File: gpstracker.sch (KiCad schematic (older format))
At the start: 16 parts, among them U1 ATMEGA328P-AU

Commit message: Major building blocks are there
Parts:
- added C?: 0.1uF, symbol C
- added ICSP: CONN_02X03, symbol CONN_02X03
- added J?: Micro_SD_Card, symbol Micro_SD_Card
- added J?: CONN_01X06, symbol CONN_01X06
- added R? (x2): 50k, symbol R
- C?: value 4.7uF -> 0.1uF
- R?: value 470R -> 10k
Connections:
- net labels added: ARD_HRX, ARD_HTX, ARD_IO10, ARD_IO7, ARD_IO8, ARD_IO9, ARD_MISO, ARD_MOSI, ARD_RST, ARD_RX, ARD_SCK, ARD_TX
- net labels removed: ARD_RXD, ARD_TXD
- wire segments 54 -> 116
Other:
- note added: "=> FTDI_VCC NOT VCC"
- note added: "SD card"

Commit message: Power supplies
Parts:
- added C? (x2): 1uF, symbol C
- added SW? (x2): SW_DPDT_x2, symbol SW_DPDT_x2
- added U?: MCP1700T-3302E/TT, symbol MCP1700T-3002E/TT
- D?: value LED -> CHRG
- D?: value LED -> DONE
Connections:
- net labels added: +3.3V, +3.3V_FDTI, +3.3V_REGUL
- net labels removed: VCC, VIN
- wire segments 116 -> 134
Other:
- note added: "GPS & GSM"
- note added: "Needs modifications for load sharing, as a starting point see :\nhttp://blog.zakkemble.co.uk/a-lithium-battery-charger-with-load-sharing/"
- note removed: "=> FTDI_VCC NOT VCC"
- note removed: "Needs modifications for load sharing, as a starting point see :\nsee http://blog.zakkemble.co.uk/a-lithium-battery-charger-with-load-sharing/"
- moved on the sheet: C?, D?, IC?, ICSP, J?, R?, SW?A, TV?, U1

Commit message: Circuitry is mostly done
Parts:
- removed J?: CONN_01X02, symbol CONN_01X02
- removed R?: 2k, symbol R
- removed R?: 470R, symbol R
- removed R?: 1k, symbol R
- removed R?: 10k, symbol R
- removed SW? (x2): SW_DPDT_x2, symbol SW_DPDT_x2
- added BT? (x2): Battery_Cell, symbol Battery_Cell
- added C? (x2): C, symbol C
- added C?: 10uF, symbol C
- added D?: D_Schottky, symbol D_Schottky
- added J? (x2): CONN_COAXIAL, symbol CONN_COAXIAL
- added J?: GS2, Connectors:GS2, symbol GS2
- added LED? (x3): LED, symbol LED
- added Q?: MOSFET_P, symbol MOSFET_P
- added R? (x2): 10k, symbol R
- added R? (x6): 1k, symbol R
- added R?: 20k, symbol R
- added R?: 160R, symbol R
- added R?: 2k, symbol R
- added R? (x2): 470R, symbol R
- added U?: 24LC512, SOIC-8_3.9x4.9mm_Pitch1.27mm, symbol 24LC512
- added U?: DS3231SN, Housings_SOIC:SOIC-16_7.5x10.3mm_Pitch1.27mm, symbol DS3231
- D? (x2): symbol LED -> LED-RESCUE-gpstracker
- R? (x2): symbol R -> R-RESCUE-gpstracker
- U?: symbol MCP73832-5-OT -> MCP73832-5-OT-RESCUE-gpstracker
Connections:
- net labels added: +2V8, +5V_FTDI, LED_NETWORK, LED_PWR, LED_SIM808_PWR, RTC_PWR, SCL, SDA, SIM808_P, SIM808_RI, SIM808_S, WAKE_UP
- net labels removed: +3.3V_FDTI, +3.3V_REGUL, ARD_IO7, ARD_IO8, ARD_IO9
- wire segments 134 -> 203
- no-connect marks 5 -> 48
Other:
- note added: "LEDs"
- note added: "Programming"
- note added: "RTC"
- note added: "Storage"
- note removed: "Needs modifications for load sharing, as a starting point see :\nhttp://blog.zakkemble.co.uk/a-lithium-battery-charger-with-load-sharing/"
- moved on the sheet: C?, D?, IC?, ICSP, J?, R?, SW?A, U1, U?

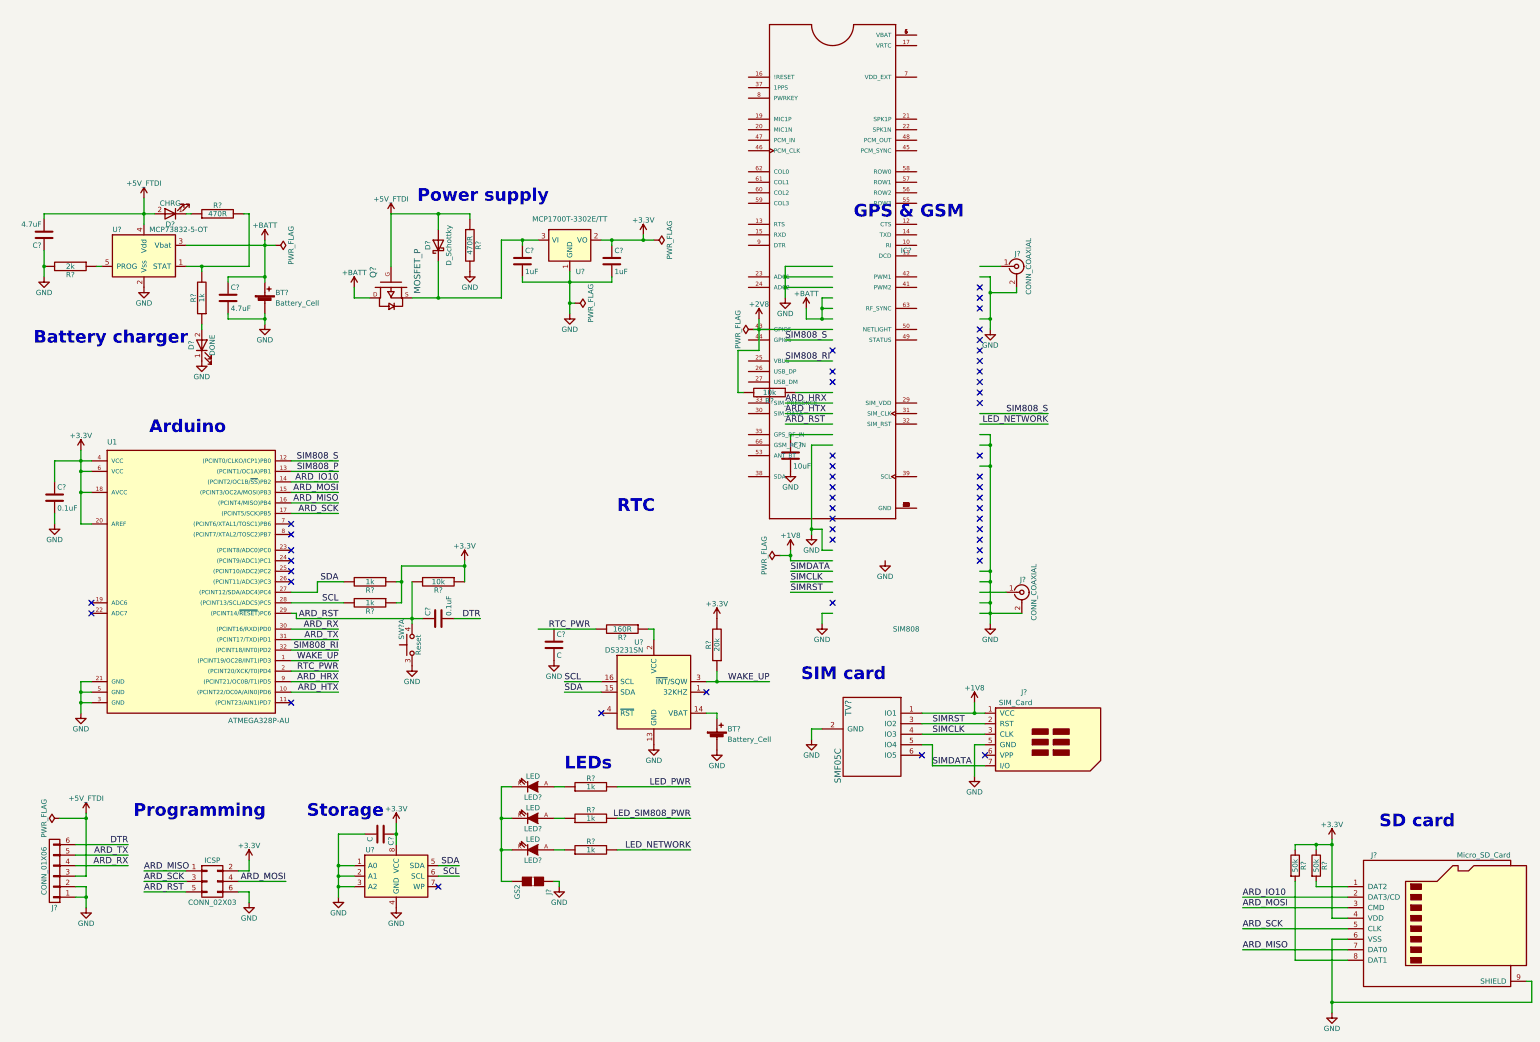
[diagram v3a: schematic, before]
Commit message: Replaced SIM808 lib with a better one
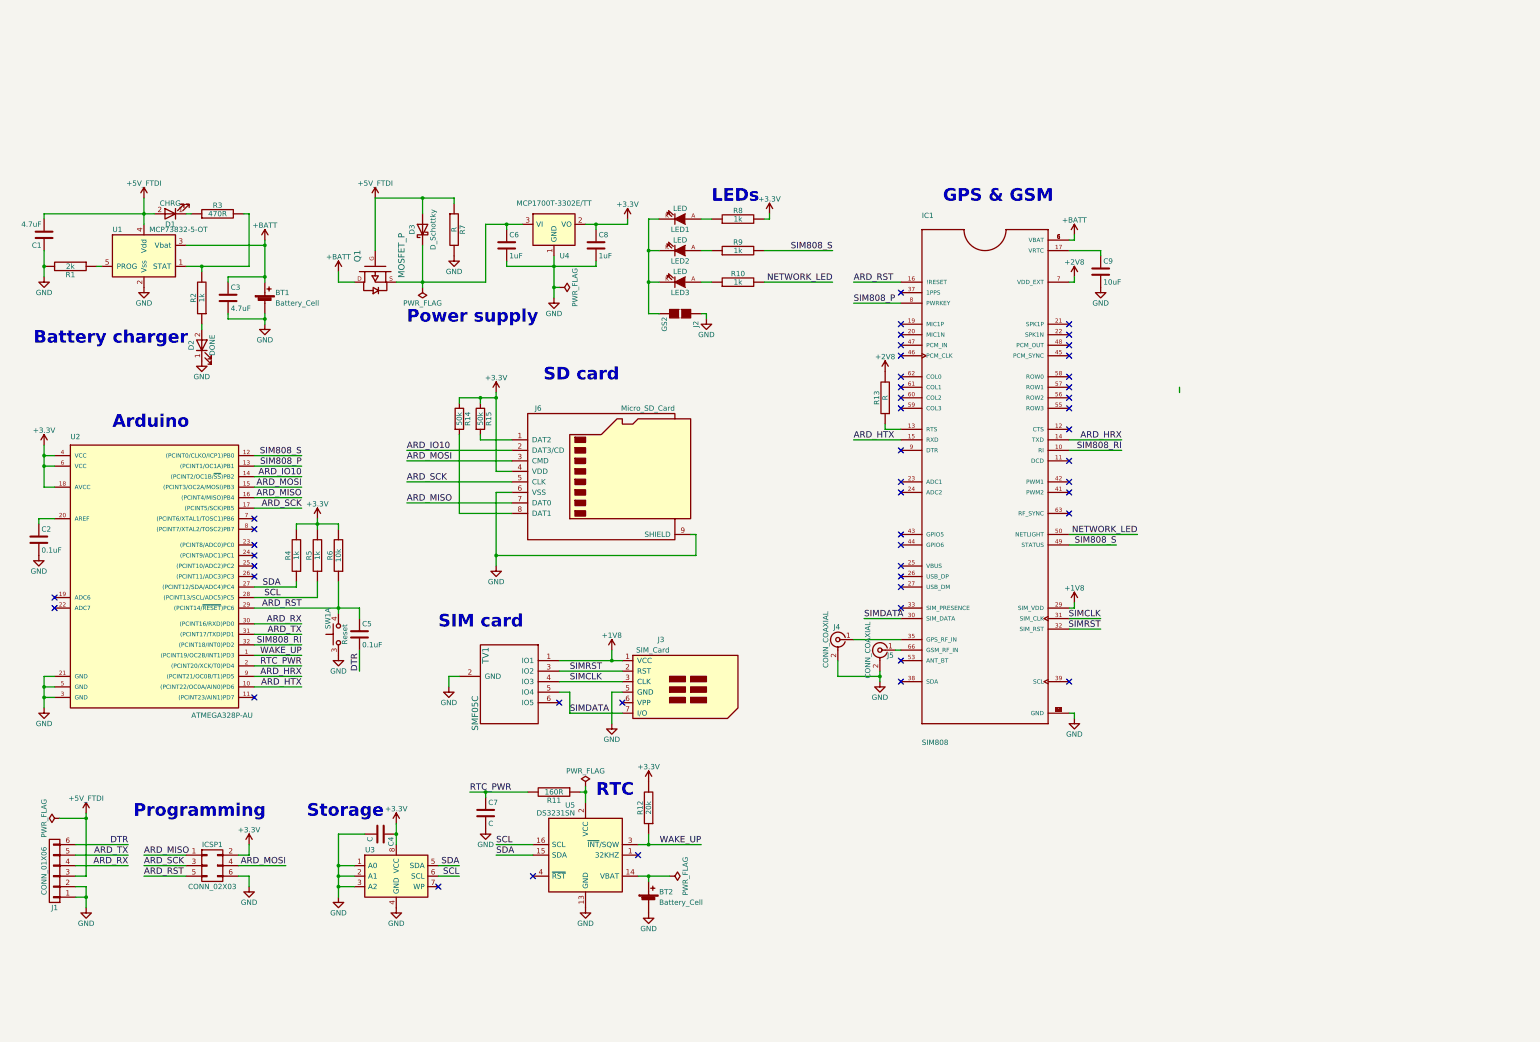
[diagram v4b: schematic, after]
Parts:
- removed C?: 10uF, symbol C
- removed IC?: SIM808, SIM808, symbol SIM808
- removed J? (x2): CONN_COAXIAL, symbol CONN_COAXIAL
- removed R?: 10k, symbol R
- added C9: 10uF, symbol C
- added IC1: SIM808, QFN100P2400X2400X260-68N, symbol SIM808
- added J4, J5: CONN_COAXIAL, symbol CONN_COAXIAL
- added R13: R, symbol R
- R7: renamed from R?; value 470R -> R
- gave numbers to parts that had none: 40
- renumbered ICSP to ICSP1, U1 to U2
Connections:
- net labels added: NETWORK_LED
- net labels removed: LED_NETWORK, LED_PWR, LED_SIM808_PWR
- wire segments 203 -> 178
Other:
- moved on the sheet: BT2, C2, C5, C6, C7, C8, D3, ICSP1, J2, J3, J6, LED1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

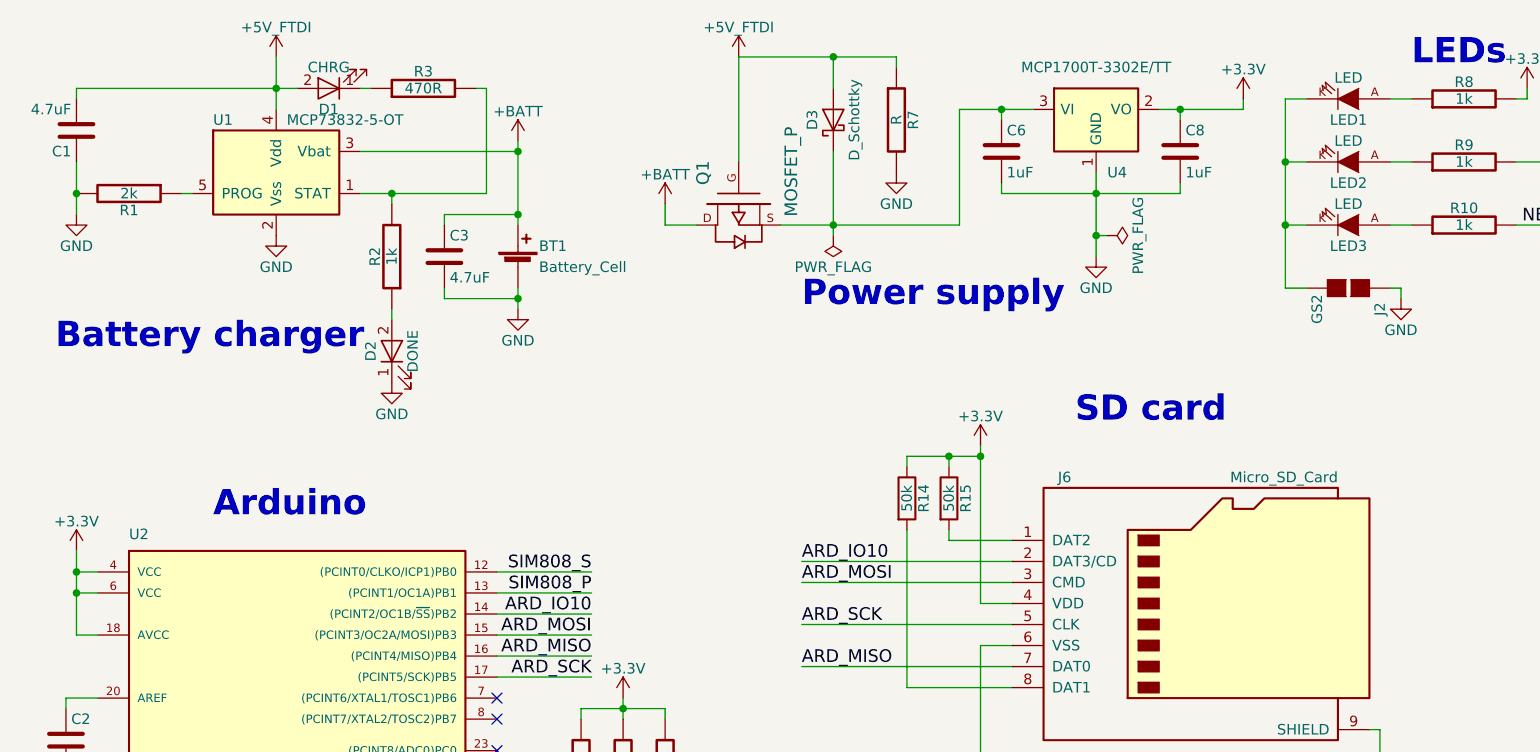
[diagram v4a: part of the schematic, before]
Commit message: Started footprints assignment
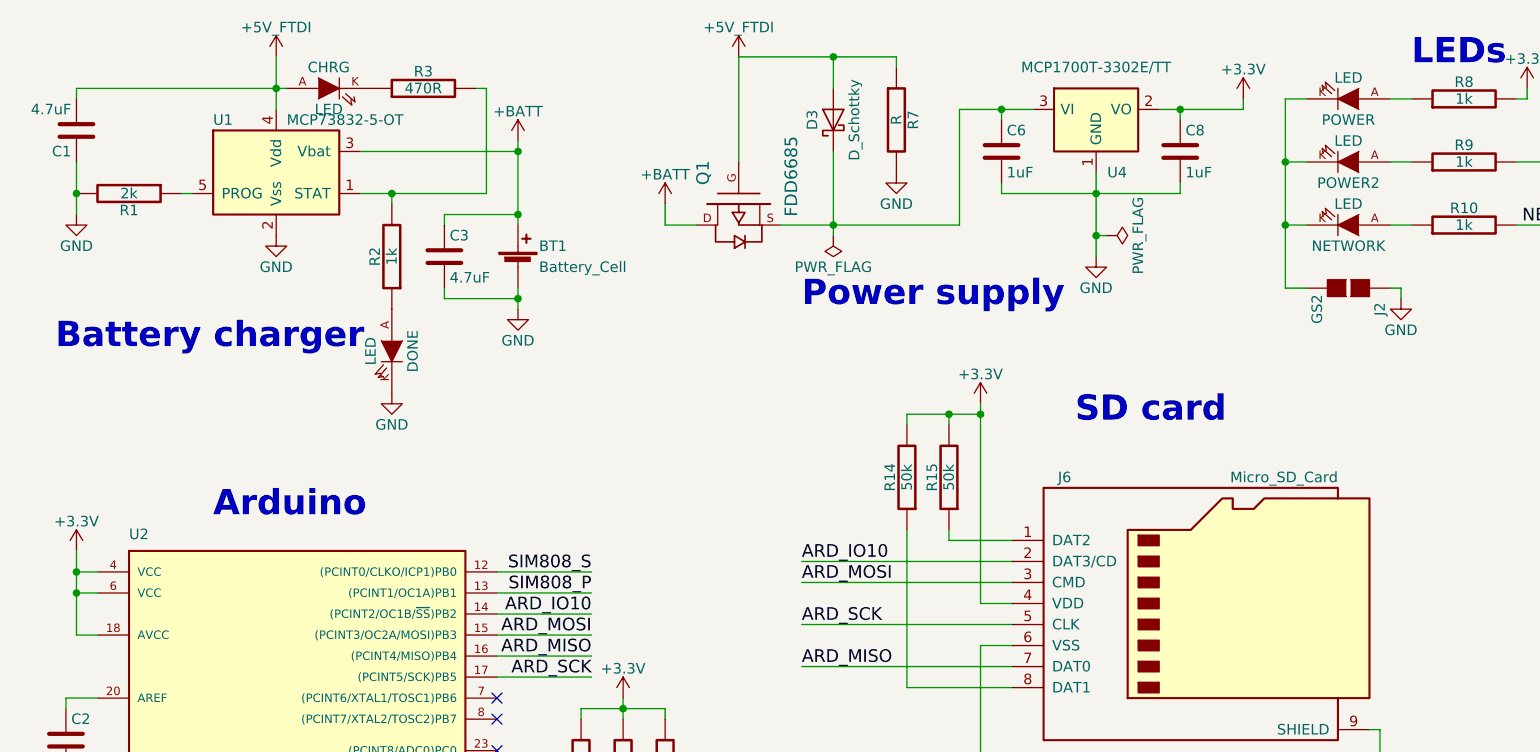
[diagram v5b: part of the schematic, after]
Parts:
- removed D1: CHRG, symbol LED-RESCUE-gpstracker
- removed D2: DONE, symbol LED-RESCUE-gpstracker
- removed R14, R15: 50k, symbol R-RESCUE-gpstracker
- added CHRG, DONE: LED, LEDs:LED_0805_HandSoldering, symbol LED
- added R14, R15: 50k, Resistors_SMD:R_0805_HandSoldering, symbol R
- C1, C2, C3, C4, C5, C6, C7, C8, C9: footprint (none) -> Capacitors_SMD:C_0805_HandSoldering
- NETWORK: renamed from LED3; footprint (none) -> LEDs:LED_0805_HandSoldering
- POWER: renamed from LED1; footprint (none) -> LEDs:LED_0805_HandSoldering
- POWER2: renamed from LED2; footprint (none) -> LEDs:LED_0805_HandSoldering
- Q1: value MOSFET_P -> FDD6685; footprint (none) -> TO_SOT_Packages_SMD:TO-252-2
- R1, R10, R11, R12, R13, R2, R3, R4, R5, R6, R7, R8, R9: footprint (none) -> Resistors_SMD:R_0805_HandSoldering
- U2: footprint TQFP32 -> Housings_QFP:TQFP-32_7x7mm_Pitch0.8mm
- U4: footprint (none) -> TO_SOT_Packages_SMD:SOT-23_Handsoldering
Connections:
- net +3V3: now also R14.2, R15.2
- net +3V3_FDTI: now also CHRG.A
- net GND: now also DONE.K
- net at R3.1: now also CHRG.K
- net at R2.1: now also DONE.A
- net at J6.1 (DAT2): now also R15.1
- net at J6.8 (DAT1): now also R14.1

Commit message: Done schematic (not verified)
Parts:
- removed J1: CONN_01X06, symbol CONN_01X06
- removed Q1: FDD6685, TO_SOT_Packages_SMD:TO-252-2, symbol MOSFET_P
- removed SW1: Reset, symbol SW_Push_Dual_x2
- added Q1: DMP1045U, TO_SOT_Packages_SMD:TO-252-2, symbol Q_PMOS_GDS
- added SW1: Reset, Buttons_Switches_SMD:SW_SPST_EVPBF, symbol SW_Push
- BT1: footprint (none) -> Connectors_JST:JST_PH_S2B-PH-SM4-TB_02x2.00mm_Angled
- BT2: footprint (none) -> Battery_Holders:Keystone_1058_1x2032-CoinCell
- C4, C7: value C -> 0.1uF
- D3: value D_Schottky -> B130LAW; footprint (none) -> Diodes_SMD:D_SOD-123
- IC1: footprint QFN100P2400X2400X260-68N -> SIM808:QFN100P2400X2400X260-68N
- ICSP1: footprint (none) -> Pin_Headers:Pin_Header_Straight_2x03_Pitch2.54mm
- J3: value SIM_Card -> 47553-0001; footprint (none) -> acronet:47553-0001
- J4, J5: footprint (none) -> Connectors_Molex:Molex_Microcoaxial_RF
- J6: footprint (none) -> 104031-0811:MOLEX_104031-0811
- LED1: renamed from CHRG; value LED -> Chg; symbol LED -> LED_ALT
- LED2: renamed from DONE; value LED -> Done; symbol LED -> LED_ALT
- LED3: renamed from POWER; value LED -> Power; symbol LED -> LED_ALT
- LED4: renamed from POWER2; value LED -> SIM_Power; symbol LED -> LED_ALT
- LED5: renamed from NETWORK; value LED -> Network; symbol LED -> LED_ALT
- R13: value R -> 10k
- R7: value R -> 100k
- TV1: footprint FT:SOT363 -> TO_SOT_Packages_SMD:SOT-363_SC-70-6_Handsoldering
- U3: footprint SOIC-8_3.9x4.9mm_Pitch1.27mm -> Housings_SOIC:SOIC-8_3.9x4.9mm_Pitch1.27mm
- U5: footprint Housings_SOIC:SOIC-16_7.5x10.3mm_Pitch1.27mm -> Housings_SOIC:SOIC-16W_7.5x10.3mm_Pitch1.27mm
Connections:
- net +BATT: now also Q1.2 (D)
- net ARD_RST: now also SW1.2
- net GND: now also LED2.1 (K), SW1.1; no longer LED2.K
- net at C6.1, D3.1 (K), U4.3 (VI): now also Q1.3 (S)
- net at R3.1: now also LED1.1 (K); no longer LED1.K
- net at R2.1: now also LED2.2 (A); no longer LED2.A
- net at R8.1: now also LED3.2 (A); no longer LED3.A
- net at R9.1: now also LED4.2 (A); no longer LED4.A
- net at R10.1: now also LED5.2 (A); no longer LED5.A
- net +3V3_FDTI renamed VBUS
- net VBUS: now also LED1.2 (A), Q1.1 (G); no longer LED1.A
- new net: J2.2 (G2), LED3.1 (K), LED4.1 (K), LED5.1 (K)
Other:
- moved on the sheet: C6, C8, D3, ICSP1, J2, R10, R7, R8, R9, U4

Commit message: Component placement
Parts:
- added C15: 0.1uF, Capacitors_SMD:C_0805_HandSoldering, symbol C
- BT1: value Battery_Cell -> External battery
- BT2: value Battery_Cell -> Backup battery
- J2: value GS2 -> Leds; footprint Connectors:GS2 -> Pin_Headers:Pin_Header_Straight_1x02_Pitch2.54mm
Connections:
- net +3V3: now also C15.1
- net GND: now also C15.2
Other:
- moved on the sheet: C2, C5, R4, R5, R6, SW1, U2

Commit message: Started routing
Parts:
- added C16: 100uF, Capacitors_Tantalum_SMD:CP_Tantalum_Case-T_EIA-3528-12_Hand, symbol CP
- added C17: 33pF, Capacitors_SMD:C_0805_HandSoldering, symbol C
- added C18: 10pF, Capacitors_SMD:C_0805_HandSoldering, symbol C
- added D1: MMSZ5231BT1G, Diodes_SMD:D_SOD-123, symbol D_Schottky
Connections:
- net +BATT: now also C16.1, C17.1, C18.1, D1.1 (K)
- net GND: now also C16.2, C17.2, C18.2, D1.2 (A)
- net RTC_PWR: now also U2.23 ((PCINT8/ADC0)PC0); no longer U2.2 ((PCINT20/XCK/T0)PD4)
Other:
- moved on the sheet: C5, R4, R5, R6, SW1
